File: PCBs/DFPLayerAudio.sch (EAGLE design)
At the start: 13 parts

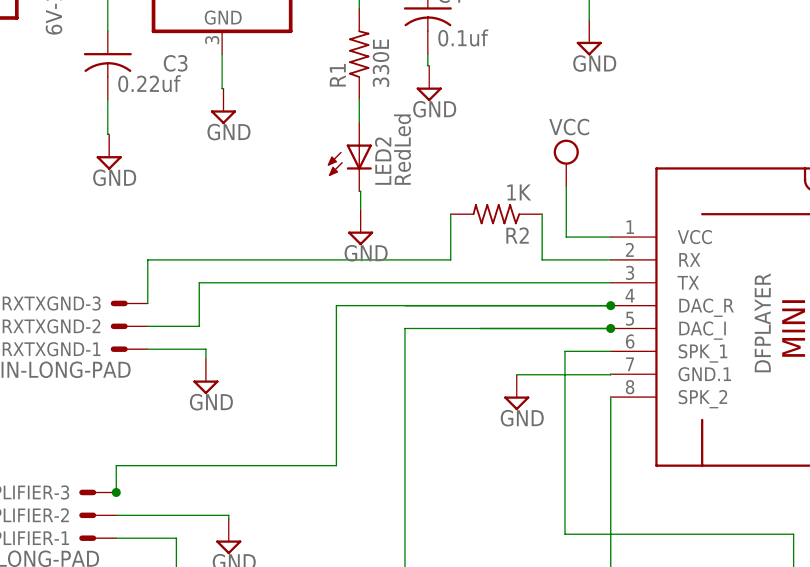
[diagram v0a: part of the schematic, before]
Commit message: TX and Rx pin updated with resistor
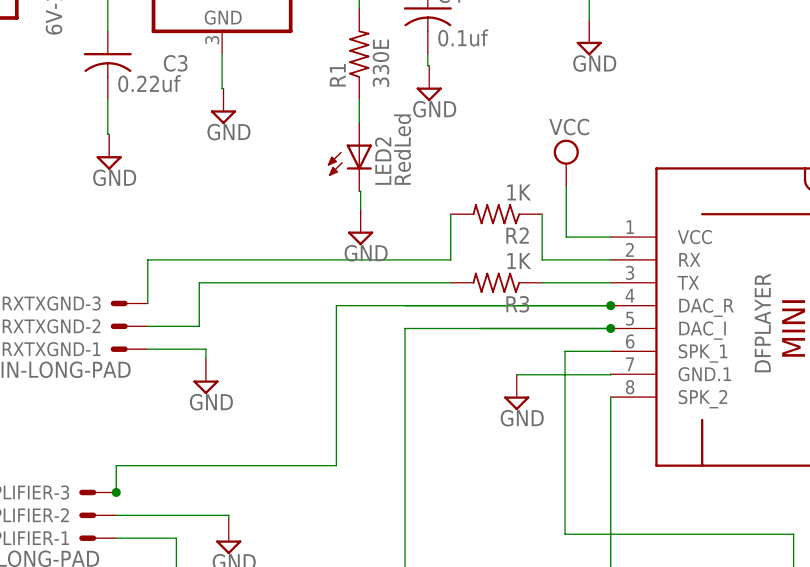
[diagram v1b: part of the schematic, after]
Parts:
- added R3: 1K, adafruit:R-US_M0805
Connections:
- new net N$4: DFPLAYER.TX, R3.1
- net N$2: now also R3.2; no longer DFPLAYER.TX
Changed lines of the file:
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@@
 <part name="5V" library="Rembrandt Electronics - JST XH Connectors v1-0" deviceset="JST-XH-02-PIN" device="-LONG-PAD"/>
 <part name="SUPPLY11" library="supply2" library_urn="urn:adsk.eagle:library:372" deviceset="GND" device=""/>
+<part name="R3" library="adafruit" deviceset="R-US_" device="M0805" value="1K"/>
 </parts>
 <sheets>
@@
 <instance part="SUPPLY11" gate="GND" x="89.052" y="74.91" smashed="yes">
 <attribute name="VALUE" x="87.147" y="71.735" size="1.778" layer="96"/>
+</instance>
+<instance part="R3" gate="G$1" x="78.74" y="48.26" smashed="yes" rot="R180">
+<attribute name="NAME" x="82.55" y="46.7614" size="1.778" layer="95" rot="R180"/>
+<attribute name="VALUE" x="82.55" y="51.562" size="1.778" layer="96" rot="R180"/>
 </instance>
 </instances>
@@
 <wire x1="40" y1="43.42" x2="45.72" y2="43.42" width="0.1524" layer="91"/>
 <wire x1="45.72" y1="43.42" x2="45.72" y2="48.26" width="0.1524" layer="91"/>
+<pinref part="R3" gate="G$1" pin="2"/>
+<wire x1="45.72" y1="48.26" x2="73.66" y2="48.26" width="0.1524" layer="91"/>
+</segment>
+</net>
+<net name="N$4" class="0">
+<segment>
+<pinref part="R3" gate="G$1" pin="1"/>
 <pinref part="DFPLAYER" gate="G$1" pin="TX"/>
-<wire x1="45.72" y1="48.26" x2="91.44" y2="48.26" width="0.1524" layer="91"/>
-</segment>
-</net>
+<wire x1="83.82" y1="48.26" x2="91.44" y2="48.26" width="0.1524" layer="91"/>
+</segment>
+</net>

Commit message: updated something
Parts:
- removed RXTXGND: JST-XH-03-PIN-LONG-PAD, Rembrandt Electronics - JST XH Connectors v1-0:JST-XH-03-PIN-LONG-PAD
- added J2: JST-XH-04-PIN-LONG-PAD, Rembrandt Electronics - JST XH Connectors v1-0:JST-XH-04-PIN-LONG-PAD
- J4: value 6V-12V -> Power
- renumbered 5V to J3, 6V-12V to J4, AMPLIFIER to J1, SPKR1 to LEFTSPKR, SPKR2 to RIGHTSPKR
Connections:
- new net N$6: DFPLAYER.BUSY, J2-2.S
- new net N$7: J2-3.S
- net GND: now also J2-1.S; no longer RXTXGND-1.S
- net N$2: no longer RXTXGND-2.S
- net N$8: now also J2-4.S; no longer RXTXGND-3.S

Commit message: audio board updated
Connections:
- removed net N$2: R3.2
- net N$7: now also R3.2
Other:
- moved on the sheet: R3
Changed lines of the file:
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@@
 <attribute name="VALUE" x="87.147" y="71.735" size="1.778" layer="96"/>
 </instance>
-<instance part="R3" gate="G$1" x="78.74" y="48.26" smashed="yes" rot="R180">
-<attribute name="NAME" x="82.55" y="46.7614" size="1.778" layer="95" rot="R180"/>
-<attribute name="VALUE" x="82.55" y="51.562" size="1.778" layer="96" rot="R180"/>
+<instance part="R3" gate="G$1" x="76.2" y="48.26" smashed="yes" rot="R180">
+<attribute name="NAME" x="80.01" y="46.7614" size="1.778" layer="95" rot="R180"/>
+<attribute name="VALUE" x="80.01" y="51.562" size="1.778" layer="96" rot="R180"/>
 </instance>
 <instance part="J2" gate="-1" x="25.4" y="38.1" smashed="yes" rot="R180">
@@
 </segment>
 </net>
-<net name="N$2" class="0">
-<segment>
-<wire x1="45.72" y1="43.42" x2="45.72" y2="48.26" width="0.1524" layer="91"/>
-<pinref part="R3" gate="G$1" pin="2"/>
-<wire x1="45.72" y1="48.26" x2="73.66" y2="48.26" width="0.1524" layer="91"/>
-</segment>
-</net>
-<net name="N$4" class="0">
-<segment>
-<pinref part="R3" gate="G$1" pin="1"/>
-<pinref part="DFPLAYER" gate="G$1" pin="TX"/>
-<wire x1="83.82" y1="48.26" x2="91.44" y2="48.26" width="0.1524" layer="91"/>
-</segment>
-</net>
 <net name="N$7" class="0">
 <segment>
 <pinref part="J2" gate="-3" pin="S"/>
 <wire x1="27.94" y1="43.18" x2="45.72" y2="43.18" width="0.1524" layer="91"/>
+<wire x1="45.72" y1="43.42" x2="45.72" y2="45.72" width="0.1524" layer="91"/>
+<pinref part="R3" gate="G$1" pin="2"/>
+<wire x1="45.72" y1="45.72" x2="45.72" y2="48.26" width="0.1524" layer="91"/>
+<wire x1="45.72" y1="48.26" x2="71.12" y2="48.26" width="0.1524" layer="91"/>
+<wire x1="45.72" y1="43.18" x2="45.72" y2="43.42" width="0.1524" layer="91"/>
 </segment>
 </net>
@@
 </segment>
 </net>
+<net name="N$4" class="0">
+<segment>
+<pinref part="R3" gate="G$1" pin="1"/>
+<pinref part="DFPLAYER" gate="G$1" pin="TX"/>
+<wire x1="81.28" y1="48.26" x2="91.44" y2="48.26" width="0.1524" layer="91"/>
+<junction x="91.44" y="48.26"/>
+</segment>
+</net>

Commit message: updated gerber and corrected few things
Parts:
- renumbered J1 to AMPLIFIER, J2 to UART, J3 to 5V, J4 to 7V-9V
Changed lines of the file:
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@@
 <part name="SUPPLY2" library="supply2" library_urn="urn:adsk.eagle:library:372" deviceset="VCC" device=""/>
 <part name="SUPPLY3" library="supply2" library_urn="urn:adsk.eagle:library:372" deviceset="VCC" device=""/>
-<part name="J4" library="SparkFun-Connectors" deviceset="CONN_02" device="5MM" value="Power"/>
+<part name="7V-9V" library="SparkFun-Connectors" deviceset="CONN_02" device="5MM" value="Power"/>
 <part name="SUPPLY4" library="supply2" library_urn="urn:adsk.eagle:library:372" deviceset="GND" device=""/>
 <part name="SUPPLY6" library="supply2" library_urn="urn:adsk.eagle:library:372" deviceset="GND" device=""/>
 <part name="SUPPLY7" library="supply2" library_urn="urn:adsk.eagle:library:372" deviceset="GND" device=""/>
 <part name="SUPPLY8" library="supply2" library_urn="urn:adsk.eagle:library:372" deviceset="GND" device=""/>
-<part name="J1" library="Rembrandt Electronics - JST XH Connectors v1-0" deviceset="JST-XH-03-PIN" device="-LONG-PAD"/>
+<part name="AMPLIFIER" library="Rembrandt Electronics - JST XH Connectors v1-0" deviceset="JST-XH-03-PIN" device="-LONG-PAD"/>
 <part name="SUPPLY9" library="supply2" library_urn="urn:adsk.eagle:library:372" deviceset="GND" device=""/>
 <part name="SUPPLY10" library="supply2" library_urn="urn:adsk.eagle:library:372" deviceset="GND" device=""/>
@@
 <part name="R2" library="adafruit" deviceset="R-US_" device="M0805" value="1K"/>
 <part name="SUPPLY5" library="supply2" library_urn="urn:adsk.eagle:library:372" deviceset="GND" device=""/>
-<part name="J3" library="Rembrandt Electronics - JST XH Connectors v1-0" deviceset="JST-XH-02-PIN" device="-LONG-PAD"/>
+<part name="5V" library="Rembrandt Electronics - JST XH Connectors v1-0" deviceset="JST-XH-02-PIN" device="-LONG-PAD"/>
 <part name="SUPPLY11" library="supply2" library_urn="urn:adsk.eagle:library:372" deviceset="GND" device=""/>
 <part name="R3" library="adafruit" deviceset="R-US_" device="M0805" value="1K"/>
-<part name="J2" library="Rembrandt Electronics - JST XH Connectors v1-0" deviceset="JST-XH-04-PIN" device="-LONG-PAD"/>
+<part name="UART" library="Rembrandt Electronics - JST XH Connectors v1-0" deviceset="JST-XH-04-PIN" device="-LONG-PAD"/>
 </parts>
 <sheets>
@@
 <attribute name="VALUE" x="84.595" y="64.675" size="1.778" layer="96"/>
 </instance>
-<instance part="J4" gate="G$1" x="21.64" y="80.22" smashed="yes">
+<instance part="7V-9V" gate="G$1" x="21.64" y="80.22" smashed="yes">
 <attribute name="VALUE" x="30.466" y="75.68" size="1.778" layer="96" font="vector" rot="R90"/>
 <attribute name="NAME" x="19.1" y="85.808" size="1.778" layer="95" font="vector"/>
@@
 <attribute name="VALUE" x="140.095" y="31.825" size="1.778" layer="96"/>
 </instance>
-<instance part="J1" gate="-1" x="33.96" y="19.88" smashed="yes" rot="R180">
+<instance part="AMPLIFIER" gate="-1" x="33.96" y="19.88" smashed="yes" rot="R180">
 <attribute name="NAME" x="31.42" y="20.642" size="1.524" layer="95" rot="R180"/>
 <attribute name="VALUE" x="34.722" y="18.483" size="1.778" layer="96" rot="R180"/>
 </instance>
-<instance part="J1" gate="-2" x="33.96" y="22.42" smashed="yes" rot="R180">
+<instance part="AMPLIFIER" gate="-2" x="33.96" y="22.42" smashed="yes" rot="R180">
 <attribute name="NAME" x="31.42" y="23.182" size="1.524" layer="95" rot="R180"/>
 </instance>
-<instance part="J1" gate="-3" x="33.96" y="24.96" smashed="yes" rot="R180">
+<instance part="AMPLIFIER" gate="-3" x="33.96" y="24.96" smashed="yes" rot="R180">
 <attribute name="NAME" x="31.42" y="25.722" size="1.524" layer="95" rot="R180"/>
 </instance>
@@
 <attribute name="VALUE" x="29.315" y="31.565" size="1.778" layer="96"/>
 </instance>
-<instance part="J3" gate="-2" x="91.44" y="81.28" smashed="yes">
+<instance part="5V" gate="-2" x="91.44" y="81.28" smashed="yes">
 <attribute name="NAME" x="93.98" y="80.518" size="1.524" layer="95"/>
 </instance>
-<instance part="J3" gate="-1" x="91.44" y="83.82" smashed="yes">
+<instance part="5V" gate="-1" x="91.44" y="83.82" smashed="yes">
 <attribute name="NAME" x="93.98" y="83.058" size="1.524" layer="95"/>
 <attribute name="VALUE" x="90.678" y="85.217" size="1.778" layer="96"/>
@@
 <attribute name="VALUE" x="80.01" y="51.562" size="1.778" layer="96" rot="R180"/>
 </instance>
-<instance part="J2" gate="-1" x="25.4" y="38.1" smashed="yes" rot="R180">
+<instance part="UART" gate="-1" x="25.4" y="38.1" smashed="yes" rot="R180">
 <attribute name="NAME" x="22.86" y="38.862" size="1.524" layer="95" rot="R180"/>
 <attribute name="VALUE" x="26.162" y="36.703" size="1.778" layer="96" rot="R180"/>
 </instance>
-<instance part="J2" gate="-2" x="25.4" y="40.64" smashed="yes" rot="R180">
+<instance part="UART" gate="-2" x="25.4" y="40.64" smashed="yes" rot="R180">
 <attribute name="NAME" x="22.86" y="41.402" size="1.524" layer="95" rot="R180"/>
 </instance>
-<instance part="J2" gate="-3" x="25.4" y="43.18" smashed="yes" rot="R180">
+<instance part="UART" gate="-3" x="25.4" y="43.18" smashed="yes" rot="R180">
 <attribute name="NAME" x="22.86" y="43.942" size="1.524" layer="95" rot="R180"/>
 </instance>
-<instance part="J2" gate="-4" x="25.4" y="45.72" smashed="yes" rot="R180">
+<instance part="UART" gate="-4" x="25.4" y="45.72" smashed="yes" rot="R180">
 <attribute name="NAME" x="22.86" y="46.482" size="1.524" layer="95" rot="R180"/>
 </instance>
@@
 </segment>
 <segment>
-<pinref part="J4" gate="G$1" pin="2"/>
+<pinref part="7V-9V" gate="G$1" pin="2"/>
 <pinref part="SUPPLY6" gate="GND" pin="GND"/>
 <wire x1="29.26" y1="82.76" x2="29.26" y2="86.48" width="0.1524" layer="91"/>
@@
 </segment>
 <segment>
-<pinref part="J1" gate="-2" pin="S"/>
+<pinref part="AMPLIFIER" gate="-2" pin="S"/>
 <pinref part="SUPPLY7" gate="GND" pin="GND"/>
 <wire x1="36.5" y1="22.42" x2="49" y2="22.42" width="0.1524" layer="91"/>
@@
 </segment>
 <segment>
-<pinref part="J3" gate="-2" pin="S"/>
+<pinref part="5V" gate="-2" pin="S"/>
 <pinref part="SUPPLY11" gate="GND" pin="GND"/>
 <wire x1="88.9" y1="81.28" x2="89.052" y2="81.28" width="0.1524" layer="91"/>
@@
 </segment>
 <segment>
-<pinref part="J2" gate="-1" pin="S"/>
+<pinref part="UART" gate="-1" pin="S"/>
 <pinref part="SUPPLY5" gate="GND" pin="GND"/>
 <wire x1="27.94" y1="38.1" x2="31.22" y2="38.1" width="0.1524" layer="91"/>
@@
 <wire x1="63.5" y1="83.82" x2="63.5" y2="81.28" width="0.1524" layer="91"/>
 <wire x1="63.5" y1="81.28" x2="71.12" y2="81.28" width="0.1524" layer="91"/>
-<pinref part="J3" gate="-1" pin="S"/>
+<pinref part="5V" gate="-1" pin="S"/>
 <wire x1="88.9" y1="83.82" x2="63.5" y2="83.82" width="0.1524" layer="91"/>
 <junction x="63.5" y="83.82"/>
@@
 <pinref part="DFPLAYER" gate="G$1" pin="DAC_I"/>
 <wire x1="91.44" y1="43.18" x2="76.962" y2="43.18" width="0.1524" layer="91"/>
-<pinref part="J1" gate="-1" pin="S"/>
+<pinref part="AMPLIFIER" gate="-1" pin="S"/>
 <wire x1="36.5" y1="19.88" x2="43.18" y2="19.88" width="0.1524" layer="91"/>
 <wire x1="43.18" y1="19.88" x2="43.18" y2="15.24" width="0.1524" layer="91"/>
@@
 <segment>
 <pinref part="7805" gate="A1" pin="VI"/>
-<pinref part="J4" gate="G$1" pin="1"/>
+<pinref part="7V-9V" gate="G$1" pin="1"/>
 <wire x1="38.1" y1="81.28" x2="35.56" y2="81.28" width="0.1524" layer="91"/>
 <wire x1="35.56" y1="81.28" x2="29.26" y2="81.28" width="0.1524" layer="91"/>
@@
 <pinref part="R2" gate="G$1" pin="2"/>
 <wire x1="73.66" y1="55.88" x2="73.66" y2="50.8" width="0.1524" layer="91"/>
-<pinref part="J2" gate="-4" pin="S"/>
+<pinref part="UART" gate="-4" pin="S"/>
 <wire x1="27.94" y1="45.72" x2="40.64" y2="45.72" width="0.1524" layer="91"/>
 <wire x1="40.64" y1="45.72" x2="40.64" y2="50.8" width="0.1524" layer="91"/>
@@
 <net name="N$1" class="0">
 <segment>
-<pinref part="J1" gate="-3" pin="S"/>
+<pinref part="AMPLIFIER" gate="-3" pin="S"/>
 <wire x1="36.5" y1="24.96" x2="36.5" y2="25.4" width="0.1524" layer="91"/>
 <wire x1="36.5" y1="24.96" x2="36.5" y2="27.94" width="0.1524" layer="91"/>
@@
 <net name="N$7" class="0">
 <segment>
-<pinref part="J2" gate="-3" pin="S"/>
+<pinref part="UART" gate="-3" pin="S"/>
 <wire x1="27.94" y1="43.18" x2="45.72" y2="43.18" width="0.1524" layer="91"/>
 <wire x1="45.72" y1="43.42" x2="45.72" y2="45.72" width="0.1524" layer="91"/>
@@
 <wire x1="114.3" y1="33.02" x2="40.64" y2="33.02" width="0.1524" layer="91"/>
 <wire x1="40.64" y1="33.02" x2="40.64" y2="40.64" width="0.1524" layer="91"/>
-<pinref part="J2" gate="-2" pin="S"/>
+<pinref part="UART" gate="-2" pin="S"/>
 <wire x1="40.64" y1="40.64" x2="27.94" y2="40.64" width="0.1524" layer="91"/>
 <pinref part="DFPLAYER" gate="G$1" pin="BUSY"/>
